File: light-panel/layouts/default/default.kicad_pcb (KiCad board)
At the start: 2 copper layers, 150 x 30 mm, 68 parts

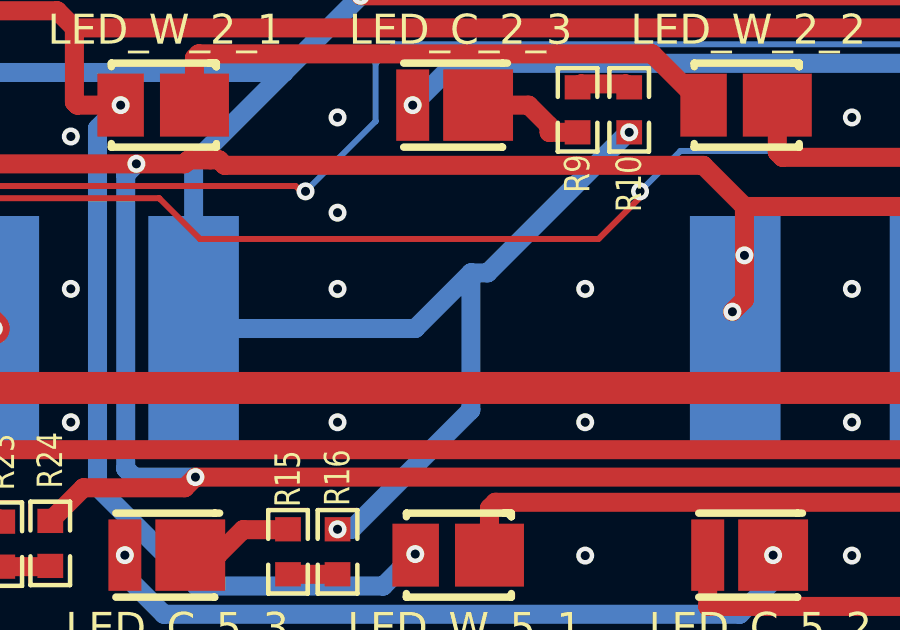
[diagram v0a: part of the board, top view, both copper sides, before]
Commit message: Added Silkscreen for export
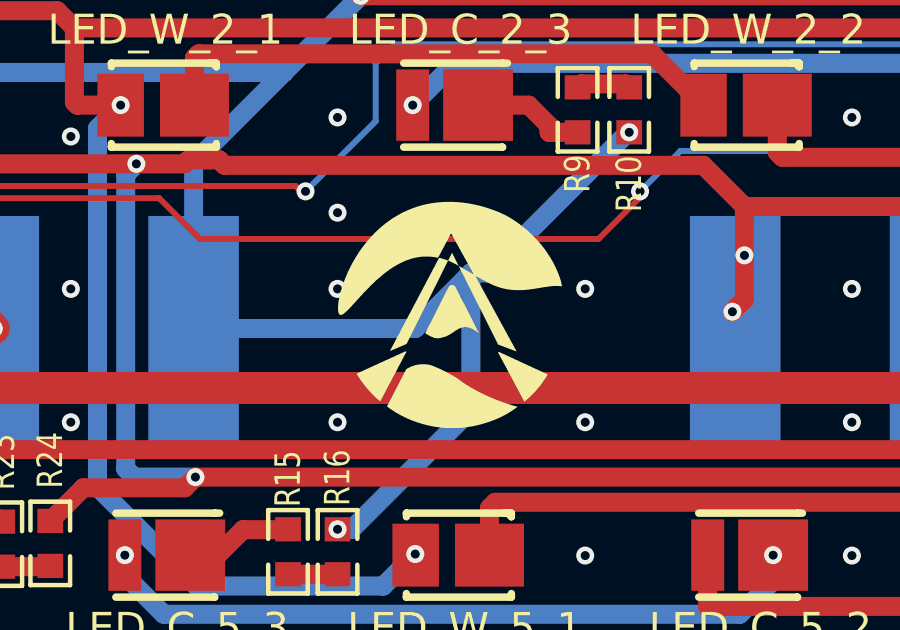
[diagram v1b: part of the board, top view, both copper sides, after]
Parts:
- added QR*****: LED-GitHub-QR-MD, Silkscreen:LED-GitHub-QR-MD, B.Cu at (208.5, 114.8)
- added REF**: KiCad-Logo2_5mm_SilkScreen, Symbol:KiCad-Logo2_5mm_SilkScreen, B.Cu at (116.2, 114.8)
- added REF**: OSHW-Logo2_7.3x6mm_SilkScreen, Symbol:OSHW-Logo2_7.3x6mm_SilkScreen, B.Cu at (129.5, 114.8)
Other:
- board text added: "LED Dual Color Panel v1.1.0 - June 2026"
